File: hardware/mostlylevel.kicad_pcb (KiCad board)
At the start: 2 copper layers, 50 x 86 mm, 31 parts, among them J1 USB-C 16P, J2 LCD QD2833 FPC, J3 CTP FT6336G FPC, J4 I2C (Qwiic), Q1 AO3400A, SW1 RESET, SW2 BOOT, U1 ESP32-S3-WROOM-1-N16R8, U2 USBLC6-2SC6, U3 ME6217C33M5G

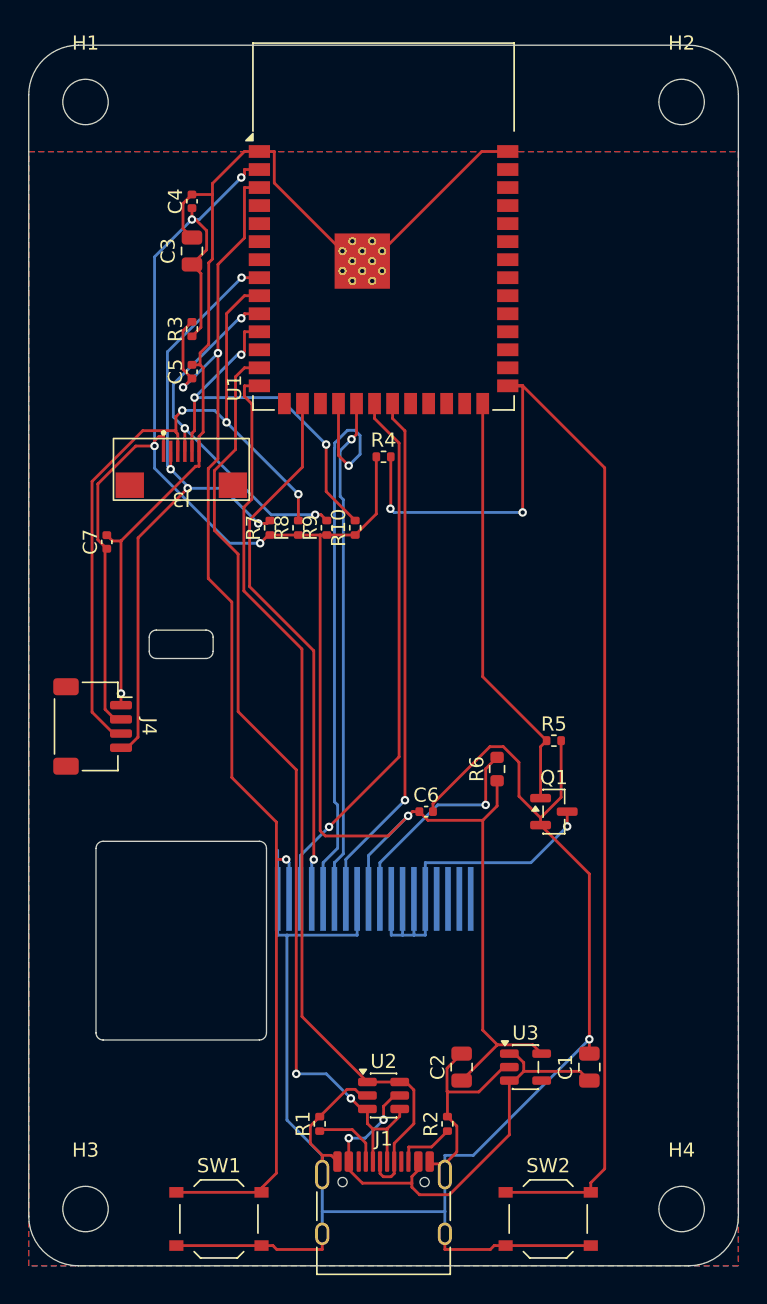
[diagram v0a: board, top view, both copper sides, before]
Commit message: Hardware: reroute the PCB for revision A (#31)
The owner's KiCad work: rerouted board, updated schematic, 22 ohm series
resistors R11/R12, and the display FPC connector J2 out of the assembly
BOM. Fabrication output moves from fab/revA-draft/ to fab/revA/ (with a
Gerber zip). routing/ keeps the DRC report of each pass, the copper
layer drawings, and the board before the reroute.

The last DRC still reports 10 errors and 4 mounting holes missing from
the schematic; see the changelog.

Co-authored-by: Claude Opus 5.5 <noreply@anthropic.com>
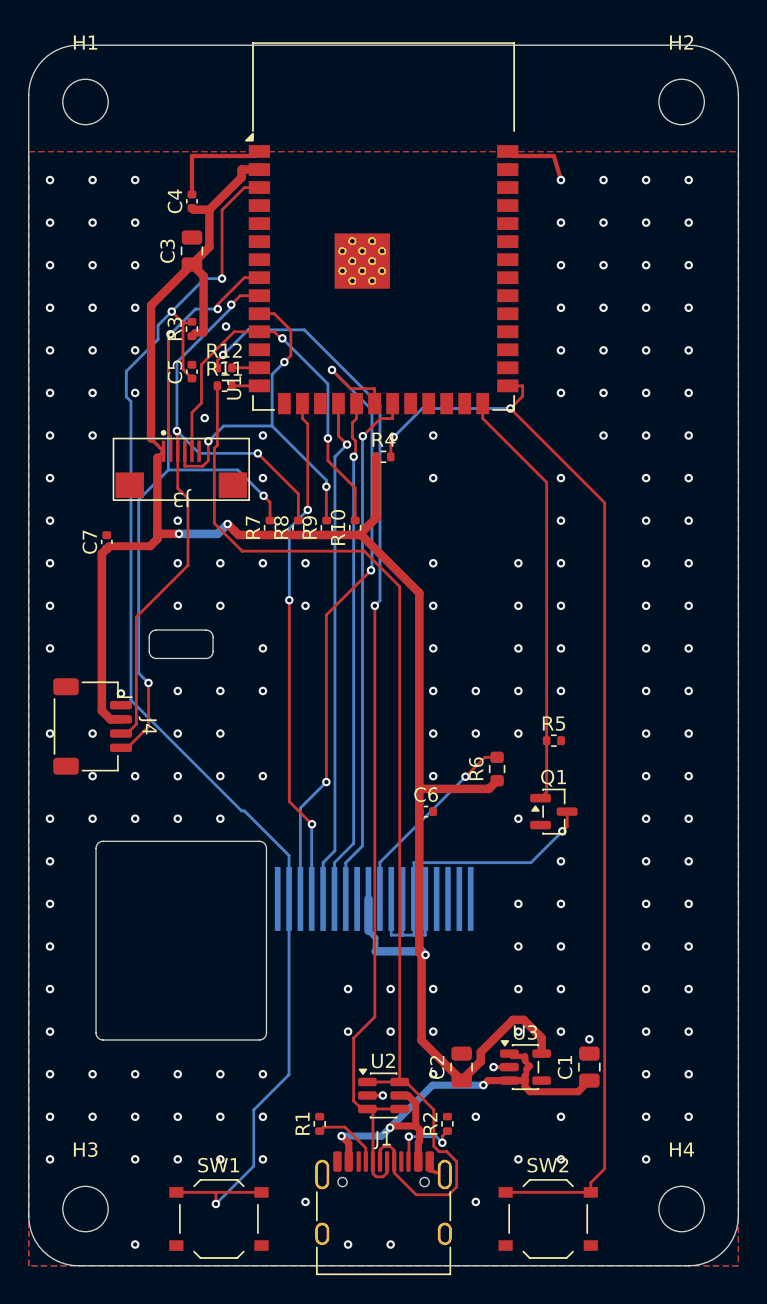
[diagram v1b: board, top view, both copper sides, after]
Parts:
- added R11: 22R, Resistor_SMD:R_0402_1005Metric, F.Cu at (113.8, 74.0)
- added R12: 22R, Resistor_SMD:R_0402_1005Metric, F.Cu at (113.8, 72.7)
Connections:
- U1 pad 13: /USB_DN -> /USB_DN_MCU
- U1 pad 14: /USB_DP -> /USB_DP_MCU
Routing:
- net /GND: track 234.2 -> 16.7 mm, vias 2 -> 188
- net /USB_DP: track 66.2 -> 80.4 mm
- net /IO0_BOOT: track 89.7 -> 77.9 mm
- net /+3V3: track 150.0 -> 140.1 mm, vias 5 -> 3
- net /I2C_SCL: track 47.5 -> 57.3 mm
- net /LCD_SCK: track 38.5 -> 45.1 mm, vias 1 -> 3
- net /LCD_CS: track 42.1 -> 35.8 mm
- net /USB_DN: track 69.0 -> 74.9 mm
- net /I2C_SDA: track 52.4 -> 48.8 mm
- net /EN: track 93.7 -> 96.6 mm
- net /VBUS: track 35.2 -> 32.6 mm, vias 2 -> 3
- net /LCD_DC: track 38.4 -> 36.3 mm, vias 1 -> 3
- net /USB_DP_MCU: track 0.00 -> 1.94 mm
- net /USB_DN_MCU: track 0.00 -> 1.94 mm
- net /CTP_INT: track 25.9 -> 27.4 mm
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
